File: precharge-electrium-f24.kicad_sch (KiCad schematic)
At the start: 14 parts, among them J1 ASMPR45-1X2-RK, J2 ASMPR45-1X2-RK, J3 B5B-PH-K-S, Q1 IRFS7530, Q2 IRFS7530, Q3 IRFS7530

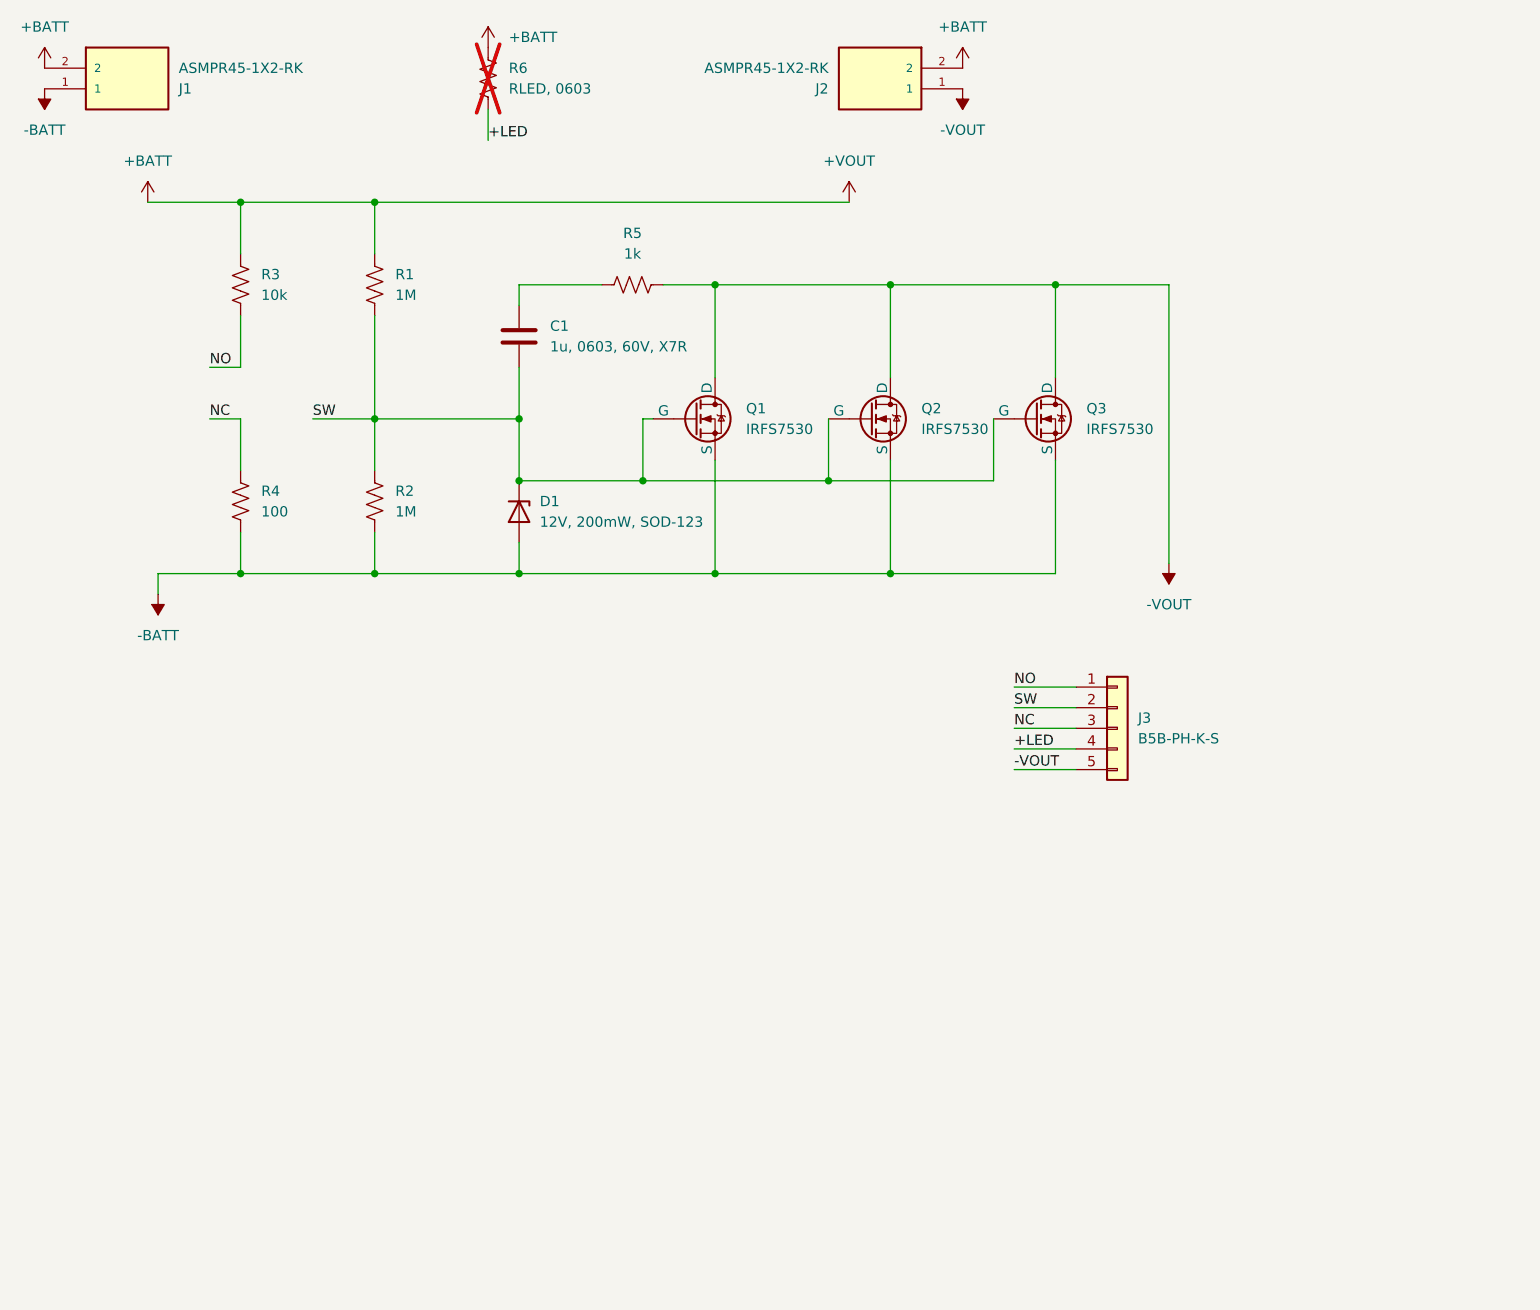
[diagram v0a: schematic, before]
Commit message: Update PCB layout and fix rules violations
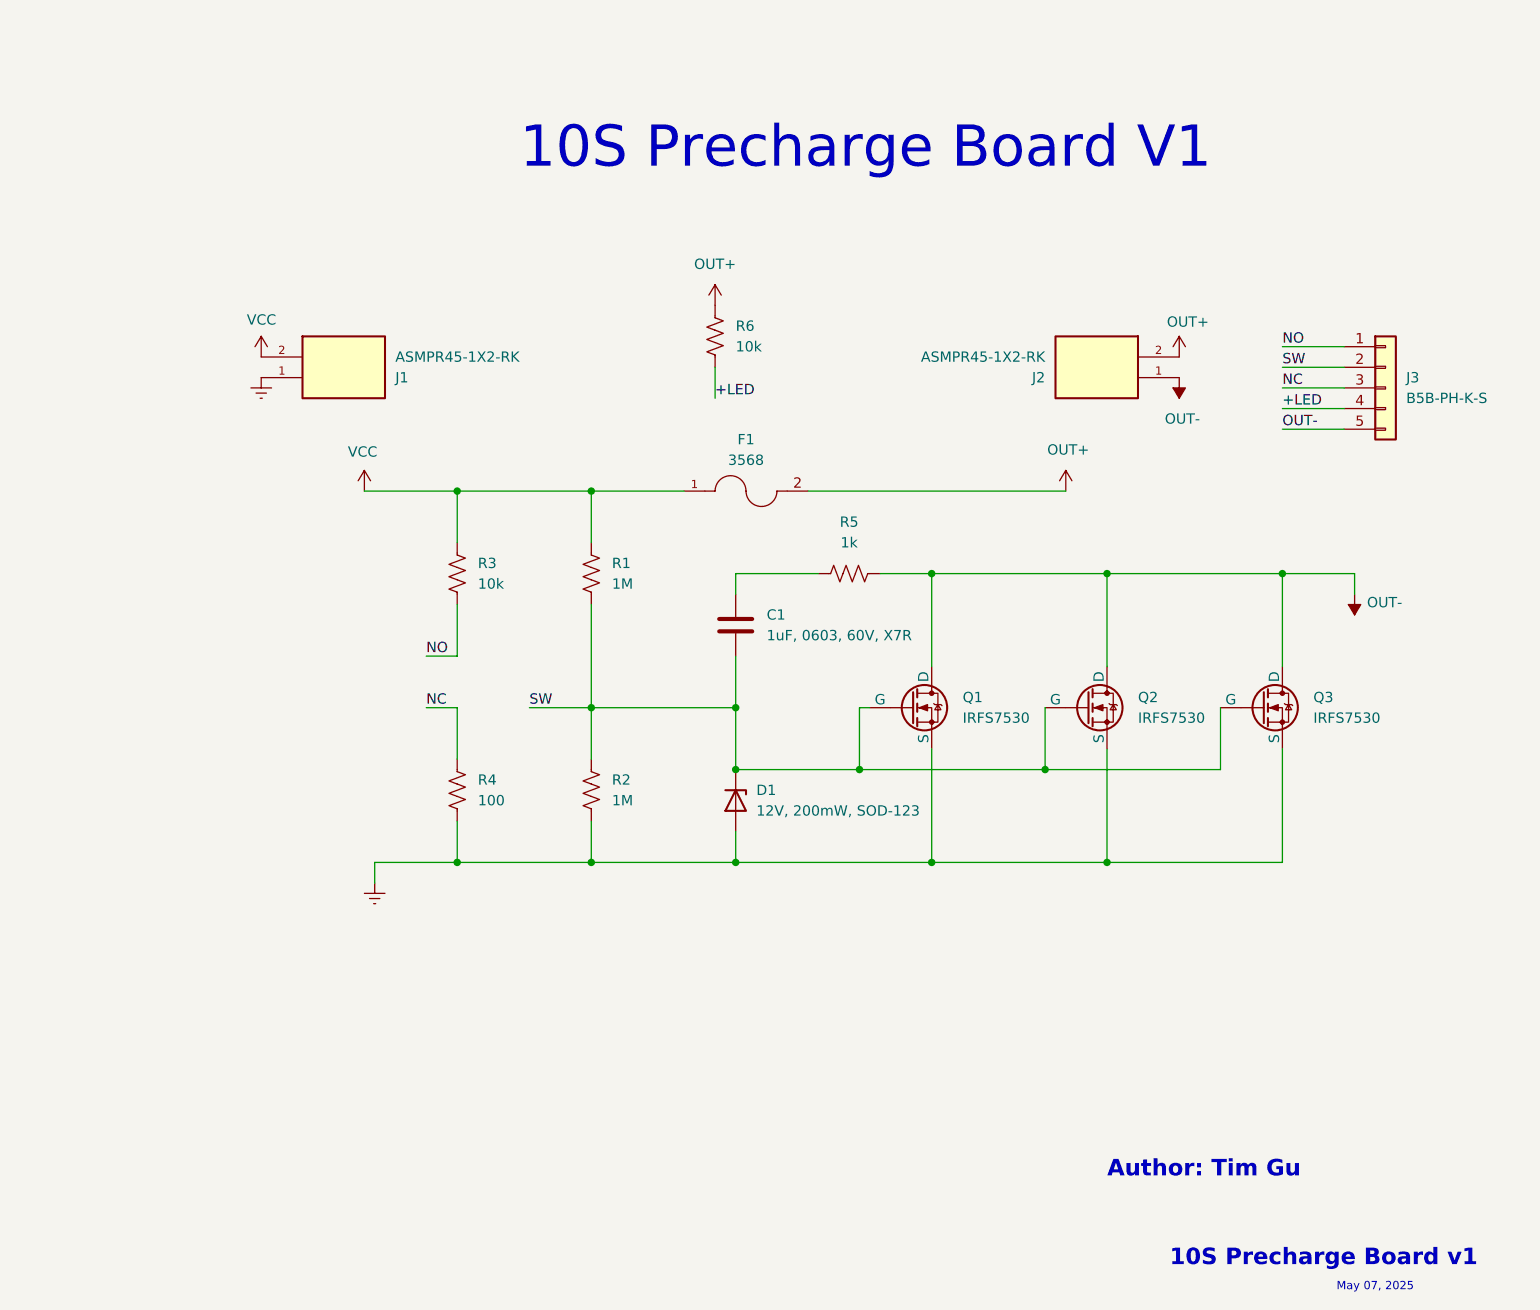
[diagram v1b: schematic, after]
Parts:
- added F1: 3568, Fuse:Fuseholder_Blade_Mini_Keystone_3568, symbol 3568:3568
- C1: value 1u, 0603, 60V, X7R -> 1uF, 0603, 60V, X7R
- R6: value RLED, 0603 -> 10k; now fitted
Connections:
- net +BATT renamed VCC
- net VCC: now also F1.1; no longer J2.2, R6.1
- net -BATT renamed GND
- net -VOUT renamed OUT-
- new net OUT+: F1.2, J2.2 (P2), R6.1
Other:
- note added: "10S Precharge Board V1"
- note added: "10S Precharge Board v1"
- note added: "Author: Tim Gu"
- note added: "May 07, 2025"
- moved on the sheet: C1, D1, J3, Q1, Q2, Q3, R1, R2, R3, R4, R5
